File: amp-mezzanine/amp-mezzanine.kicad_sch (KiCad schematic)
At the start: 26 parts, among them J1 LOGIC_IN, J2 I2C

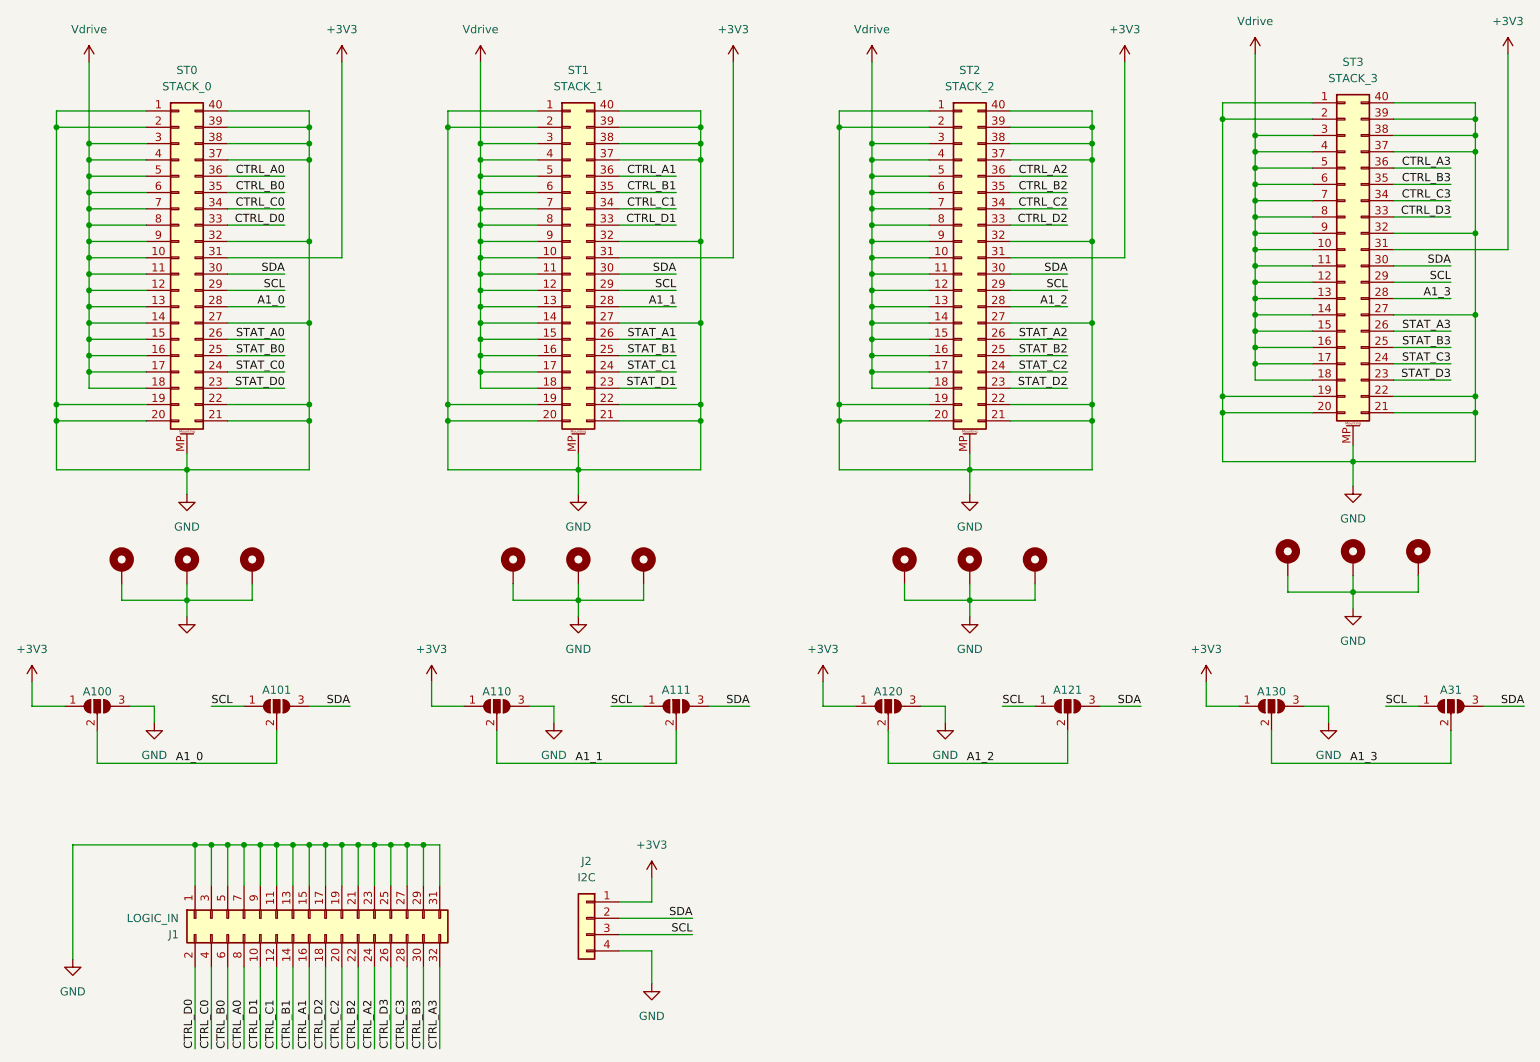
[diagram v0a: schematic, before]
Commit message: Finished mezzanine layout
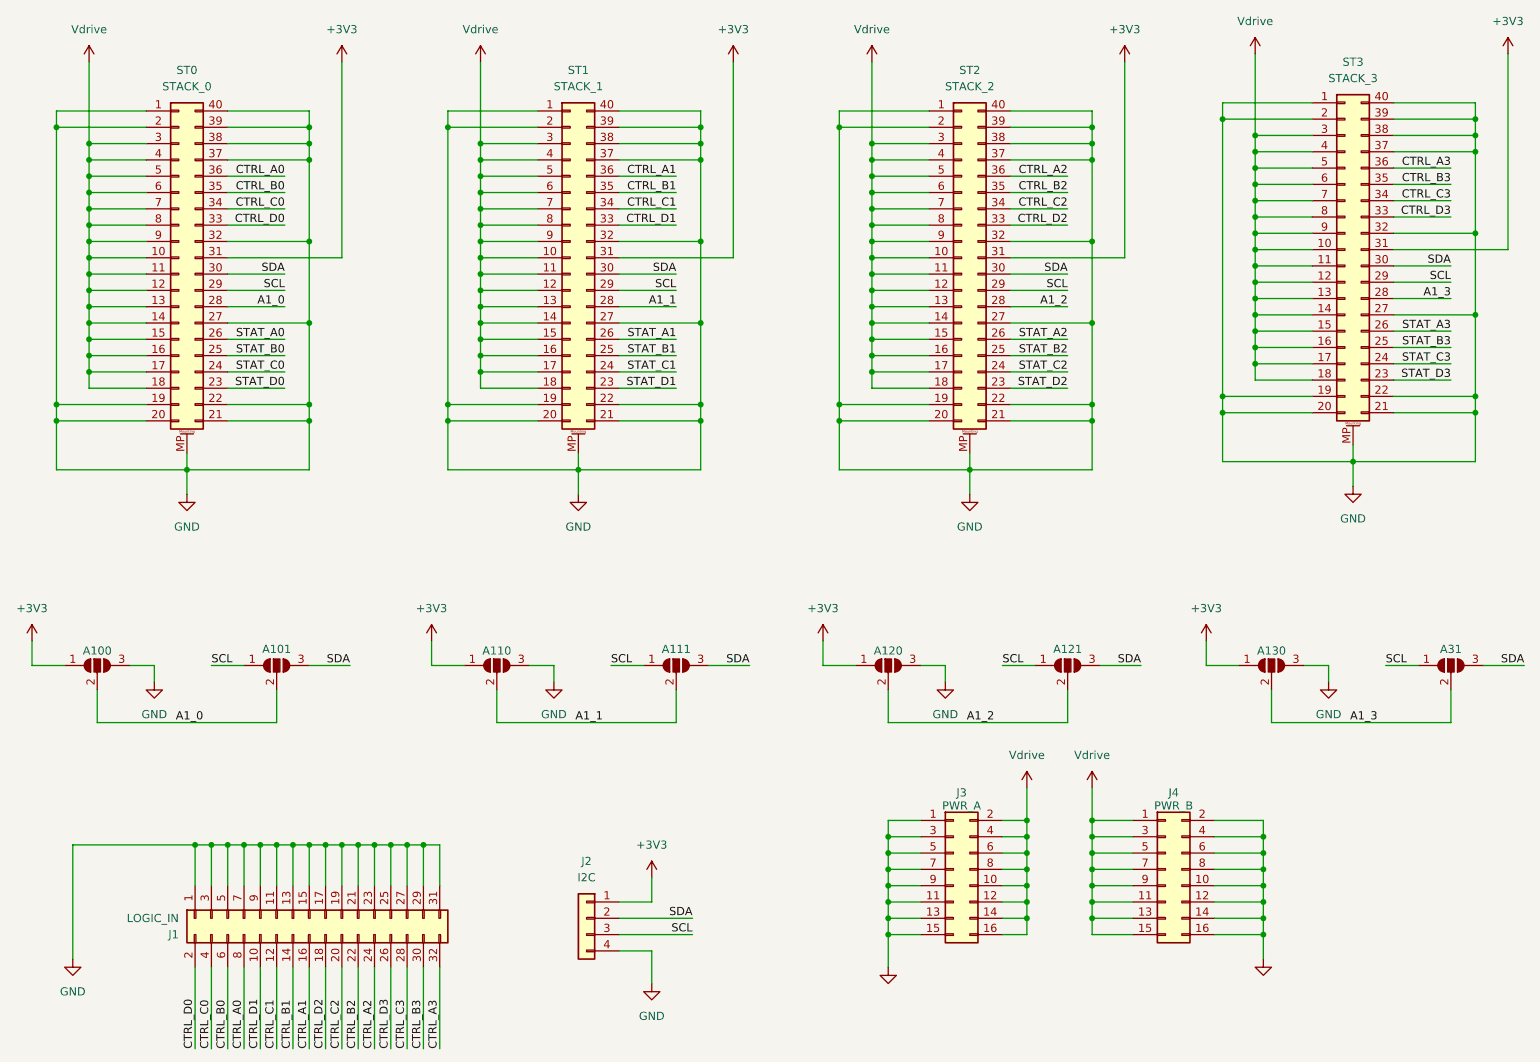
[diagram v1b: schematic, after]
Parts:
- removed H1, H10, H11, H12, H2, H3, H4, H5, H6, H7, H8, H9: MountingHole_Pad, MountingHole:MountingHole_3.2mm_M3_Pad_Via, symbol Mechanical:MountingHole_Pad
- added J3: PWR_A, Connector_PinHeader_2.54mm:PinHeader_2x08_P2.54mm_Vertical, symbol Connector_Generic:Conn_02x08_Odd_Even
- added J4: PWR_B, Connector_PinHeader_2.54mm:PinHeader_2x08_P2.54mm_Vertical, symbol Connector_Generic:Conn_02x08_Odd_Even
- ST0, ST1, ST2, ST3: footprint project_footprints:AMPHENOL_10132797-045100LF -> project_footprints:PICCDAC-AMPHENOL-10132797-045100LF
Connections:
- net GND: now also J3.1 (Pin_1), J3.11 (Pin_11), J3.13 (Pin_13), J3.15 (Pin_15), J3.3 (Pin_3), J3.5 (Pin_5), J3.7 (Pin_7), J3.9 (Pin_9), J4.10 (Pin_10), J4.12 (Pin_12), J4.14 (Pin_14), J4.16 (Pin_16), J4.2 (Pin_2), J4.4 (Pin_4), J4.6 (Pin_6), J4.8 (Pin_8)
- net Vdrive: now also J3.10 (Pin_10), J3.12 (Pin_12), J3.14 (Pin_14), J3.16 (Pin_16), J3.2 (Pin_2), J3.4 (Pin_4), J3.6 (Pin_6), J3.8 (Pin_8), J4.1 (Pin_1), J4.11 (Pin_11), J4.13 (Pin_13), J4.15 (Pin_15), J4.3 (Pin_3), J4.5 (Pin_5), J4.7 (Pin_7), J4.9 (Pin_9)
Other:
- moved on the sheet: A100, A101, A110, A111, A120, A121, A130, A31
